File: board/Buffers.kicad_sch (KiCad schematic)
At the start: 8 parts, among them U58 74F541, U59 74F245, U60 74F541, U61 74F125

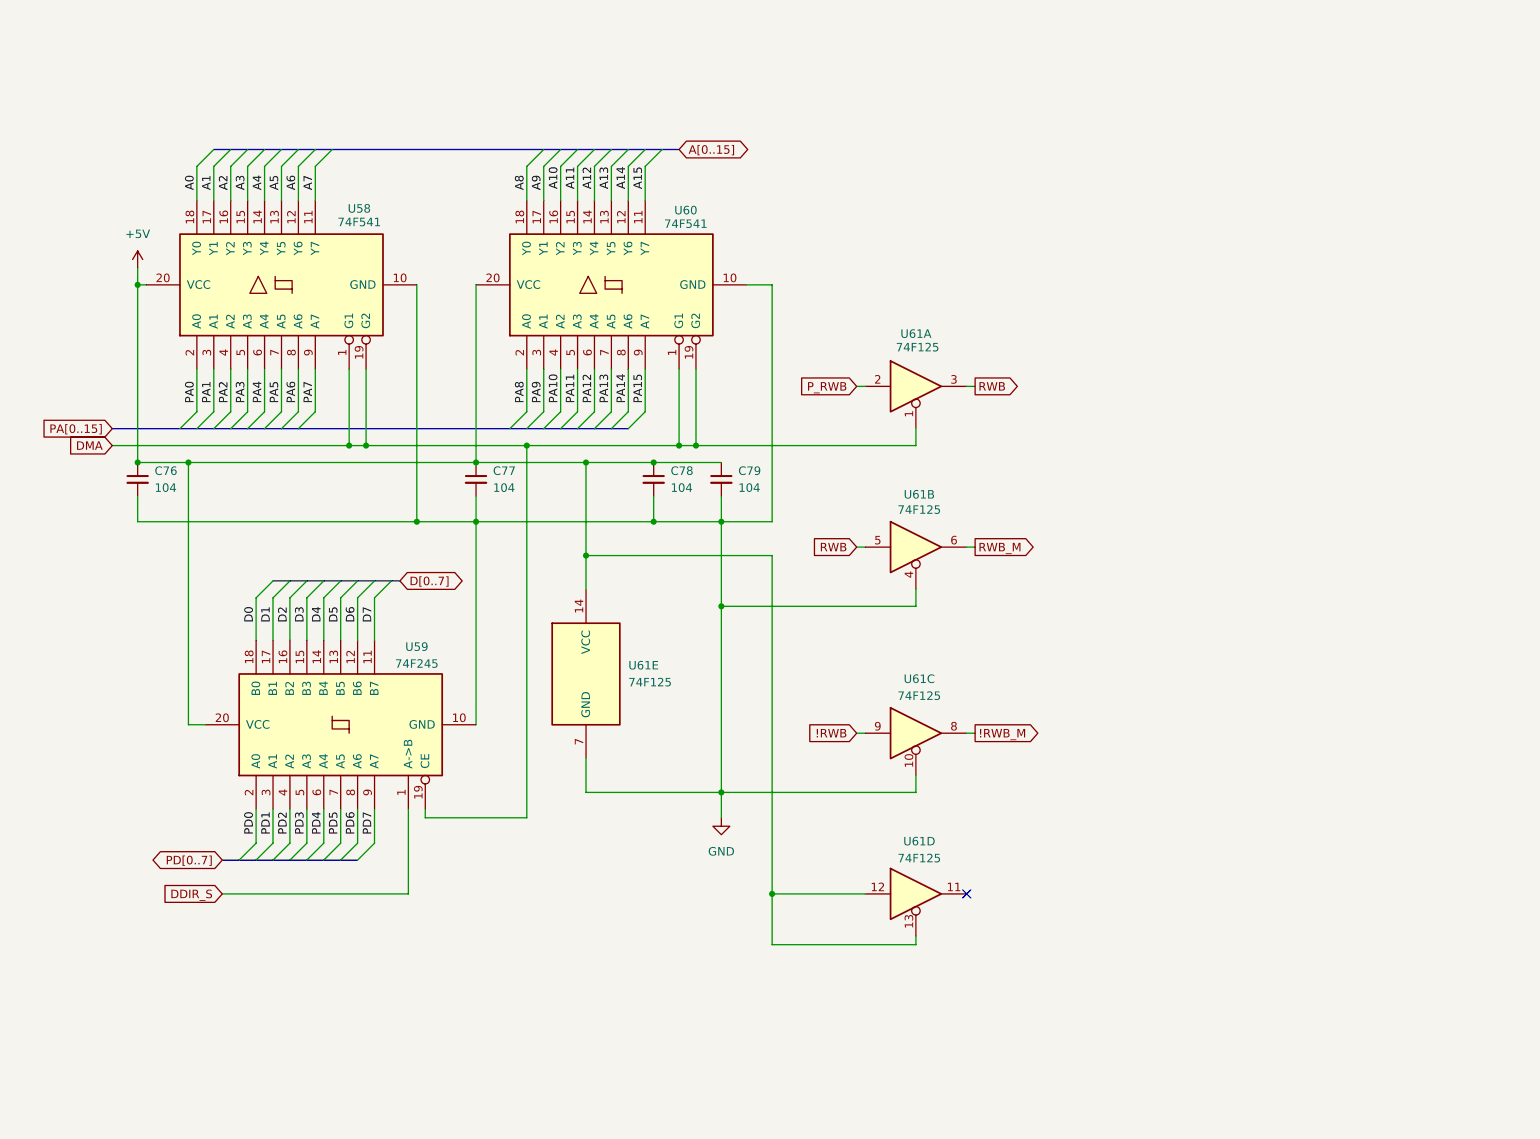
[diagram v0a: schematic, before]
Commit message: V2.0 changes with new S register and simplified logic
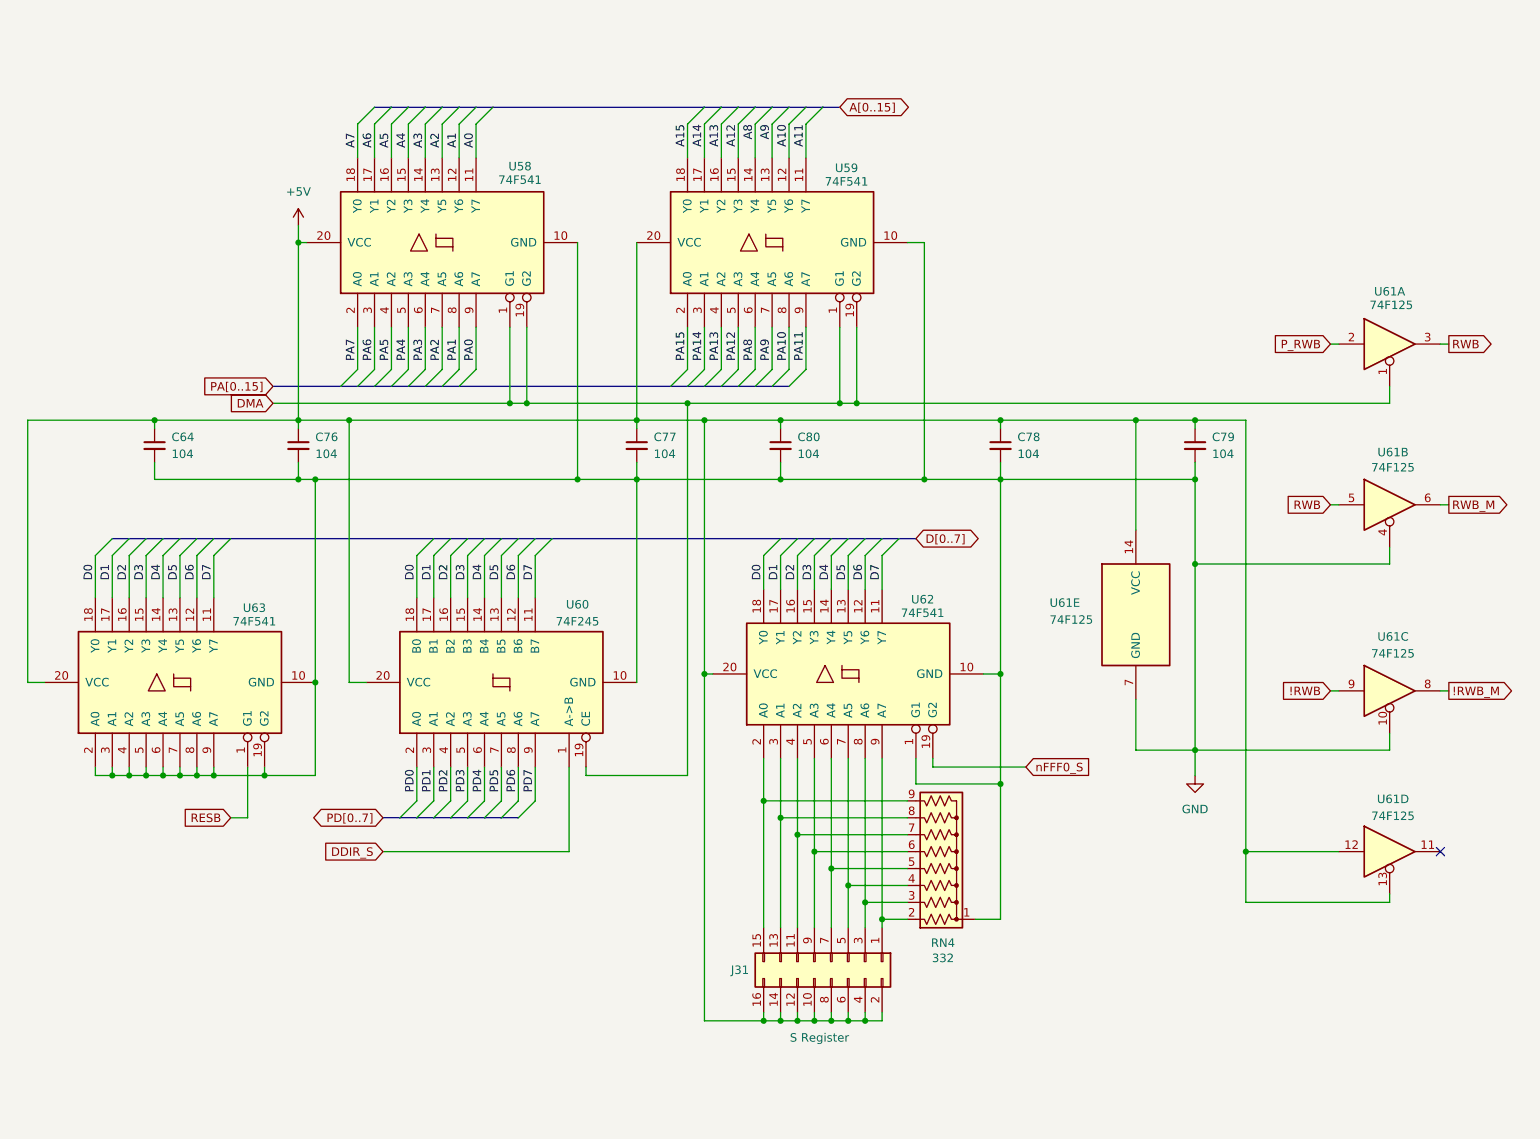
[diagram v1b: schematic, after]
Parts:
- added C64, C80: 104, Capacitor_THT:C_Disc_D5.0mm_W2.5mm_P5.00mm, symbol Device:C_Small
- added J31: S Register, Connector_PinHeader_2.54mm:PinHeader_2x08_P2.54mm_Vertical, symbol Connector_Generic:Conn_02x08_Odd_Even
- added RN4: 332, Resistor_THT:R_Array_SIP9, symbol Device:R_Network08_US
- added U62, U63: 74F541, Package_DIP:DIP-20_W7.62mm_Socket_LongPads, symbol 74xx:74LS541
- renumbered U60 to U59, U59 to U60
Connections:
- net +5V: now also C64.1, C80.1, J31.10 (Pin_10), J31.12 (Pin_12), J31.14 (Pin_14), J31.16 (Pin_16), J31.2 (Pin_2), J31.4 (Pin_4), J31.6 (Pin_6), J31.8 (Pin_8), U62.20 (VCC), U63.20 (VCC)
- net A0: now also U58.11 (Y7); no longer U58.18 (Y0)
- net A1: now also U58.12 (Y6); no longer U58.17 (Y1)
- net A10: now also U59.12 (Y6); no longer U59.16 (Y2)
- net A11: now also U59.11 (Y7); no longer U59.15 (Y3)
- net A12: now also U59.15 (Y3); no longer U59.14 (Y4)
- net A13: now also U59.16 (Y2); no longer U59.13 (Y5)
- net A14: now also U59.17 (Y1); no longer U59.12 (Y6)
- net A15: now also U59.18 (Y0); no longer U59.11 (Y7)
- net A2: now also U58.13 (Y5); no longer U58.16 (Y2)
- net A3: now also U58.14 (Y4); no longer U58.15 (Y3)
- net A4: now also U58.15 (Y3); no longer U58.14 (Y4)
- net A5: now also U58.16 (Y2); no longer U58.13 (Y5)
- net A6: now also U58.17 (Y1); no longer U58.12 (Y6)
- net A7: now also U58.18 (Y0); no longer U58.11 (Y7)
- net A8: now also U59.14 (Y4); no longer U59.18 (Y0)
- net A9: now also U59.13 (Y5); no longer U59.17 (Y1)
- net D0: now also U62.18 (Y0), U63.18 (Y0)
- net D1: now also U62.17 (Y1), U63.17 (Y1)
- net D2: now also U62.16 (Y2), U63.16 (Y2)
- net D3: now also U62.15 (Y3), U63.15 (Y3)
- net D4: now also U62.14 (Y4), U63.14 (Y4)
- net D5: now also U62.13 (Y5), U63.13 (Y5)
- net D6: now also U62.12 (Y6), U63.12 (Y6)
- net D7: now also U62.11 (Y7), U63.11 (Y7)
- net GND: now also C64.2, C80.2, RN4.1 (common), U62.1 (G1), U62.10 (GND), U63.10 (GND), U63.19 (G2), U63.2 (A0), U63.3 (A1), U63.4 (A2), U63.5 (A3), U63.6 (A4), U63.7 (A5), U63.8 (A6), U63.9 (A7)
- net PA0: now also U58.9 (A7); no longer U58.2 (A0)
- net PA1: now also U58.8 (A6); no longer U58.3 (A1)
- net PA10: now also U59.8 (A6); no longer U59.4 (A2)
- net PA11: now also U59.9 (A7); no longer U59.5 (A3)
- net PA12: now also U59.5 (A3); no longer U59.6 (A4)
- net PA13: now also U59.4 (A2); no longer U59.7 (A5)
- net PA14: now also U59.3 (A1); no longer U59.8 (A6)
- net PA15: now also U59.2 (A0); no longer U59.9 (A7)
- net PA2: now also U58.7 (A5); no longer U58.4 (A2)
- net PA3: now also U58.6 (A4); no longer U58.5 (A3)
- net PA4: now also U58.5 (A3); no longer U58.6 (A4)
- net PA5: now also U58.4 (A2); no longer U58.7 (A5)
- net PA6: now also U58.3 (A1); no longer U58.8 (A6)
- net PA7: now also U58.2 (A0); no longer U58.9 (A7)
- net PA8: now also U59.6 (A4); no longer U59.2 (A0)
- net PA9: now also U59.7 (A5); no longer U59.3 (A1)
- new net: J31.1 (Pin_1), RN4.2 (R1), U62.9 (A7)
- new net: J31.11 (Pin_11), RN4.7 (R6), U62.4 (A2)
- new net: J31.13 (Pin_13), RN4.8 (R7), U62.3 (A1)
- new net: J31.15 (Pin_15), RN4.9 (R8), U62.2 (A0)
- new net: J31.3 (Pin_3), RN4.3 (R2), U62.8 (A6)
- new net: J31.5 (Pin_5), RN4.4 (R3), U62.7 (A5)
- new net: J31.7 (Pin_7), RN4.5 (R4), U62.6 (A4)
- new net: J31.9 (Pin_9), RN4.6 (R5), U62.5 (A3)
- new net RESB: U63.1 (G1)
- new net nFFF0_S: U62.19 (G2)
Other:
- moved on the sheet: C76, C77, C78, C79, U58, U59, U60, U61A, U61B, U61C, U61D, U61E

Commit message: V2.0 updates and new hydra breakout and counter cards.
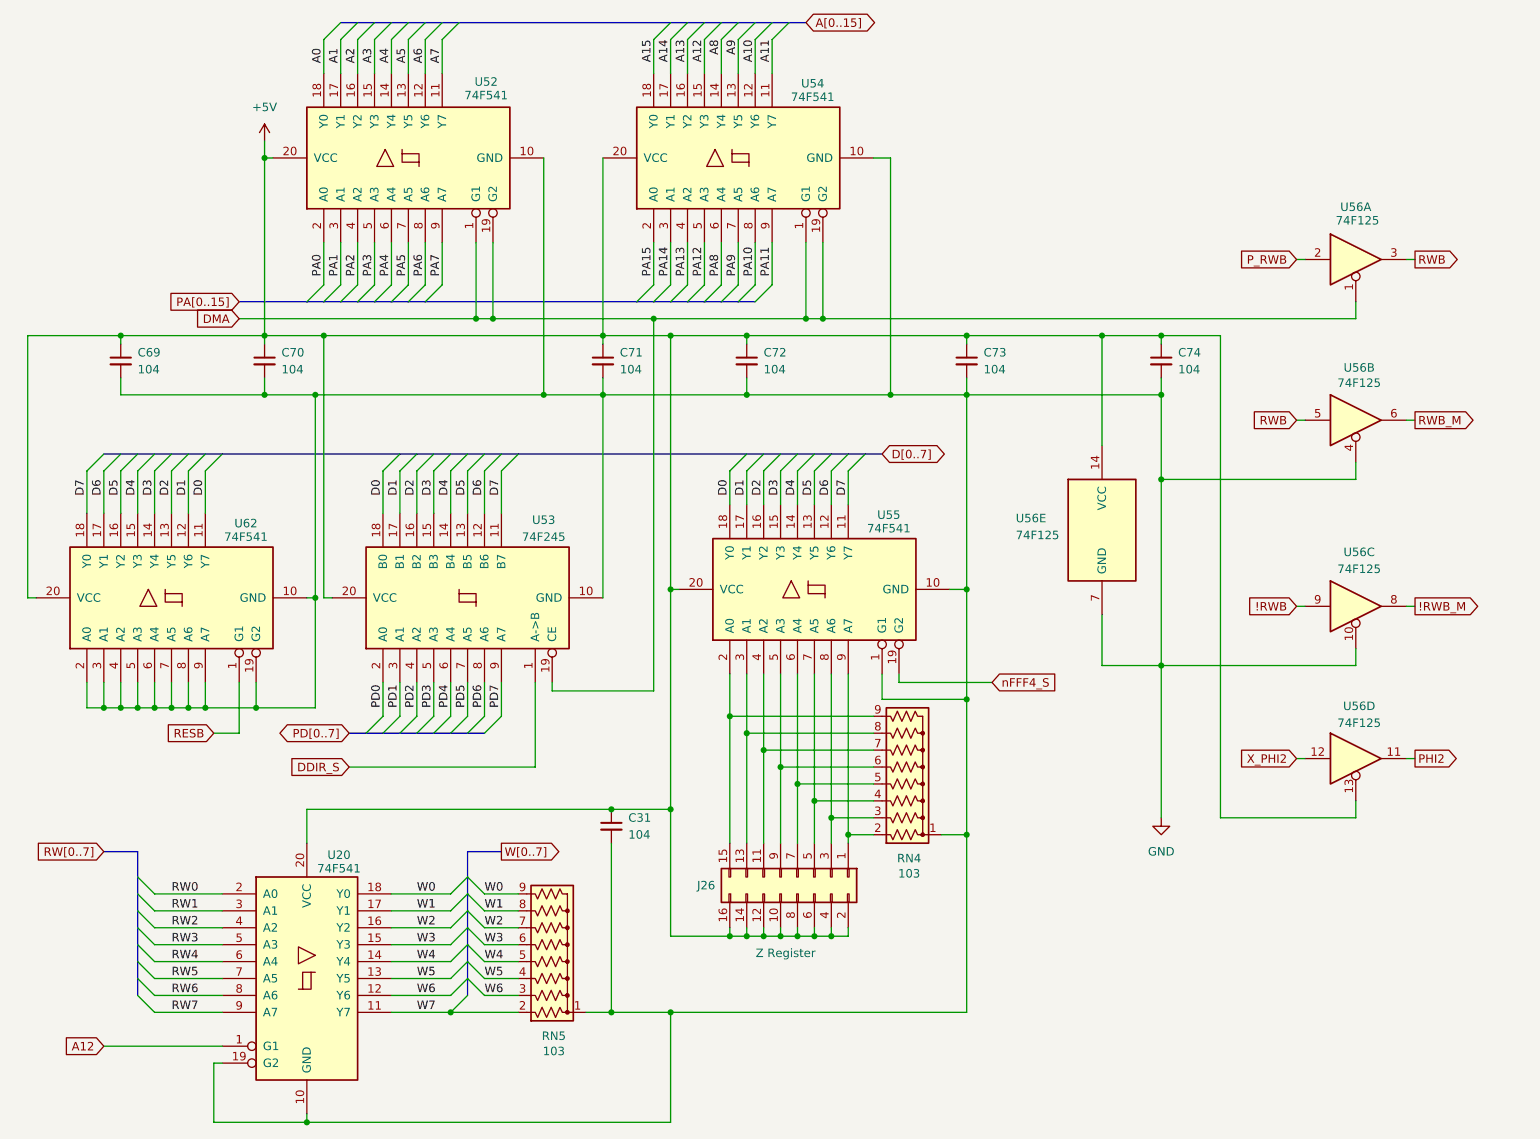
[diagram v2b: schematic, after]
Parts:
- removed unit 4 of U61
- removed U63: 74F541, Package_DIP:DIP-20_W7.62mm_Socket_LongPads, symbol 74xx:74LS541
- added C31: 104, Capacitor_THT:C_Disc_D5.0mm_W2.5mm_P5.00mm, symbol Device:C_Small
- added RN5: 103, Resistor_THT:R_Array_SIP9, symbol Device:R_Network08_US
- added U20, U62: 74F541, Package_DIP:DIP-20_W7.62mm_Socket_LongPads, symbol 74xx:74LS541
- added unit 4 of U56
- J26: renamed from J31; value S Register -> Z Register
- RN4: value 332 -> 103
- renumbered C64 to C69, C76 to C70, C77 to C71, C80 to C72, C78 to C73, C79 to C74, U58 to U52, U60 to U53, U59 to U54, U62 to U55, U61 to U56
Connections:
- net +5V: now also C31.1, U20.20 (VCC), U56.13, U62.20 (VCC)
- net A0: now also U52.18 (Y0); no longer U52.11 (Y7)
- net A1: now also U52.17 (Y1); no longer U52.12 (Y6)
- net A12: now also U20.1 (G1)
- net A2: now also U52.16 (Y2); no longer U52.13 (Y5)
- net A3: now also U52.15 (Y3); no longer U52.14 (Y4)
- net A4: now also U52.14 (Y4); no longer U52.15 (Y3)
- net A5: now also U52.13 (Y5); no longer U52.16 (Y2)
- net A6: now also U52.12 (Y6); no longer U52.17 (Y1)
- net A7: now also U52.11 (Y7); no longer U52.18 (Y0)
- net D0: now also U62.11 (Y7)
- net D1: now also U62.12 (Y6)
- net D2: now also U62.13 (Y5)
- net D3: now also U62.14 (Y4)
- net D4: now also U62.15 (Y3)
- net D5: now also U62.16 (Y2)
- net D6: now also U62.17 (Y1)
- net D7: now also U62.18 (Y0)
- net GND: now also C31.2, RN5.1 (common), U20.10 (GND), U20.19 (G2), U62.10 (GND), U62.19 (G2), U62.2 (A0), U62.3 (A1), U62.4 (A2), U62.5 (A3), U62.6 (A4), U62.7 (A5), U62.8 (A6), U62.9 (A7)
- net PA0: now also U52.2 (A0); no longer U52.9 (A7)
- net PA1: now also U52.3 (A1); no longer U52.8 (A6)
- net PA2: now also U52.4 (A2); no longer U52.7 (A5)
- net PA3: now also U52.5 (A3); no longer U52.6 (A4)
- net PA4: now also U52.6 (A4); no longer U52.5 (A3)
- net PA5: now also U52.7 (A5); no longer U52.4 (A2)
- net PA6: now also U52.8 (A6); no longer U52.3 (A1)
- net PA7: now also U52.9 (A7); no longer U52.2 (A0)
- net RESB: now also U62.1 (G1)
- net nFFF0_S renamed nFFF4_S
- new net PHI2: U56.11
- new net RW0: U20.2 (A0)
- new net RW1: U20.3 (A1)
- new net RW2: U20.4 (A2)
- new net RW3: U20.5 (A3)
- new net RW4: U20.6 (A4)
- new net RW5: U20.7 (A5)
- new net RW6: U20.8 (A6)
- new net RW7: U20.9 (A7)
- new net W0: RN5.9 (R8), U20.18 (Y0)
- new net W1: RN5.8 (R7), U20.17 (Y1)
- new net W2: RN5.7 (R6), U20.16 (Y2)
- new net W3: RN5.6 (R5), U20.15 (Y3)
- new net W4: RN5.5 (R4), U20.14 (Y4)
- new net W5: RN5.4 (R3), U20.13 (Y5)
- new net W6: RN5.3 (R2), U20.12 (Y6)
- new net W7: RN5.2 (R1), U20.11 (Y7)
- new net X_PHI2: U56.12
- no-connect marks 1 -> 0
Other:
- title: Buffers & Mixer -> ZeroPage $00/$01 Mirror Memory and RAM/ROM Bank Logic
- moved on the sheet: C69, C70, C71, C72, C73, C74, J26, RN4, U52, U53, U54, U55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
